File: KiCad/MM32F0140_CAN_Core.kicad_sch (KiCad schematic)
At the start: 1 part, among them U1 PIC32MX110F016D-IPT

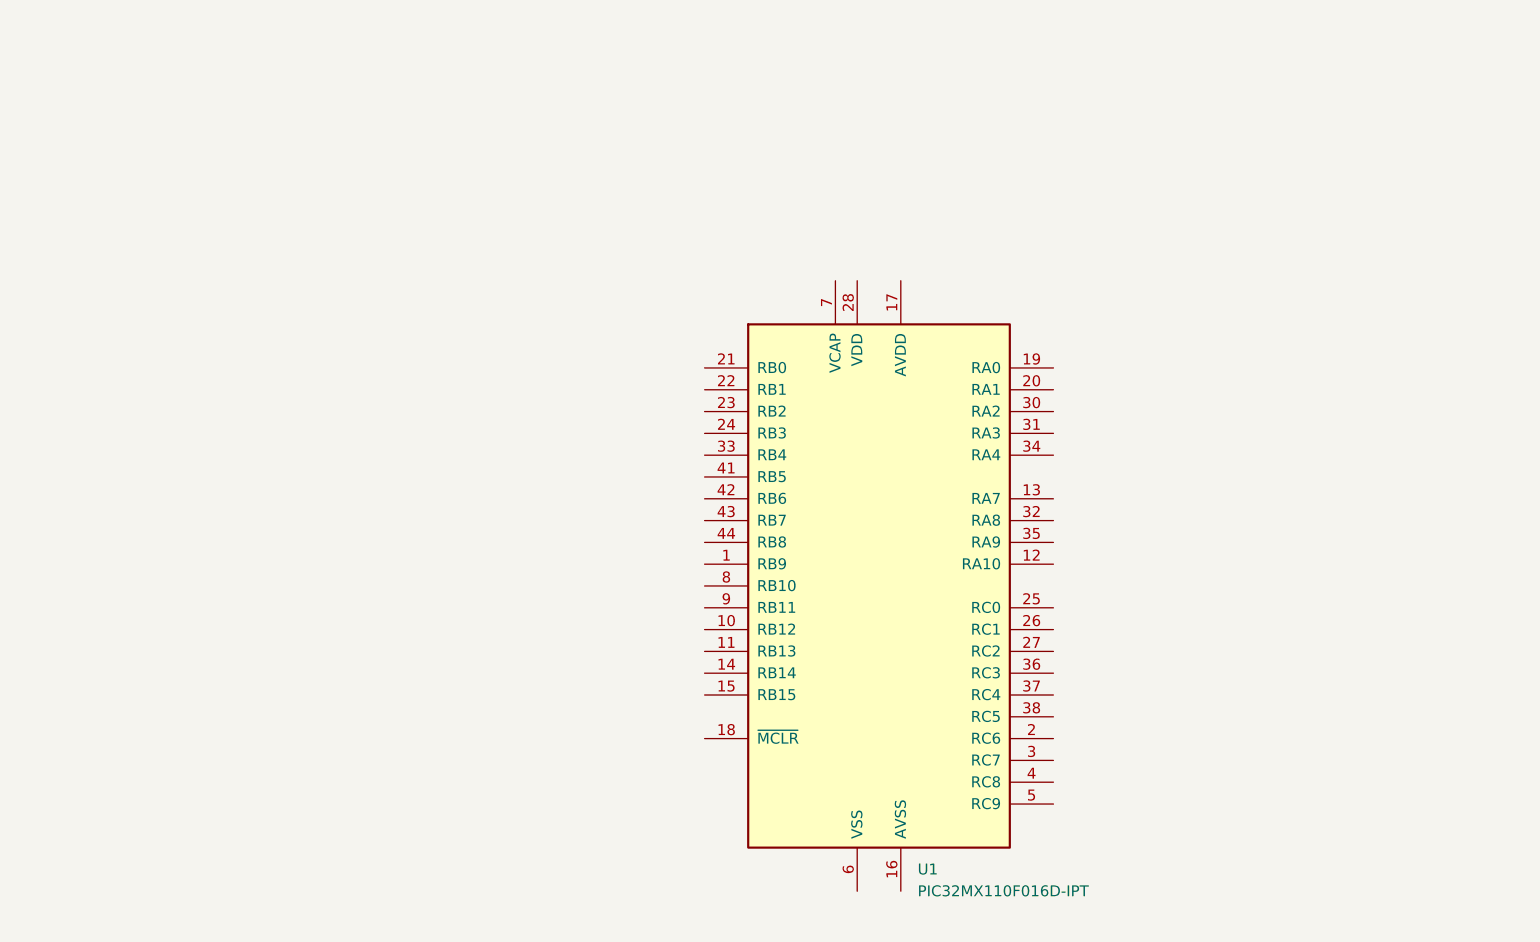
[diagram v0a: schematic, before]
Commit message: 更新原理图
23.4.7
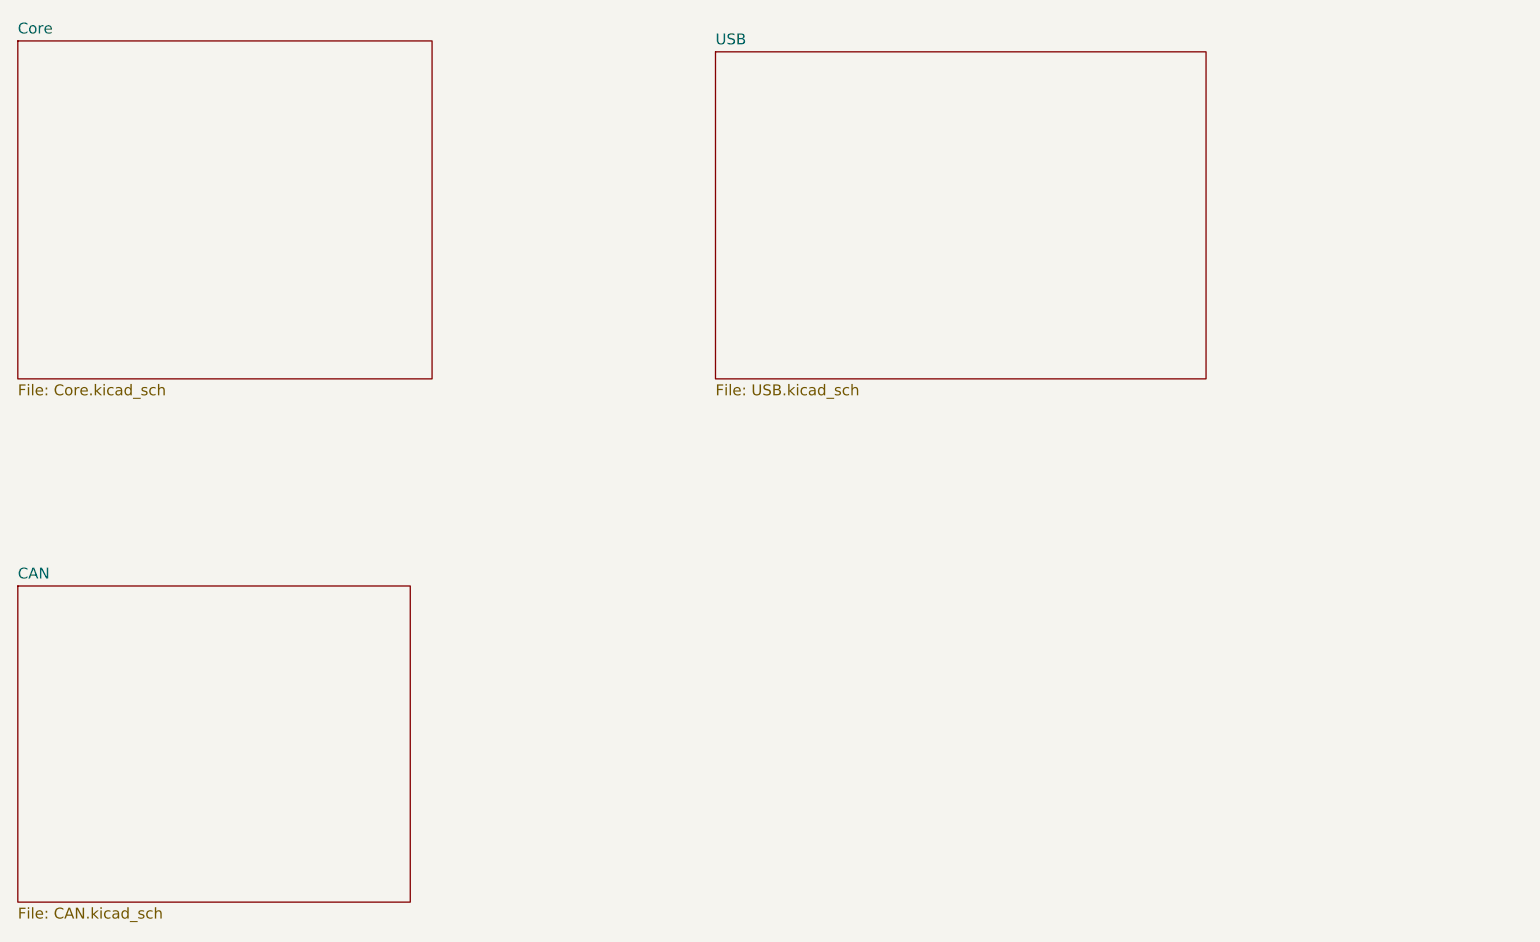
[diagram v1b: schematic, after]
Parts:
- removed U1: PIC32MX110F016D-IPT, Package_QFP:TQFP-44_10x10mm_P0.8mm, symbol MCU_Microchip_PIC32:PIC32MX110F016D-IPT
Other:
- added sheet CAN (CAN.kicad_sch)
- added sheet Core (Core.kicad_sch)
- added sheet USB (USB.kicad_sch)
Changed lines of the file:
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@@
 (kicad_sch (version 20230121) (generator eeschema)
   (paper "A4")
-  (symbol (lib_id "MCU_Microchip_PIC32:PIC32MX110F016D-IPT") (at 132.08 85.09 0) (unit 1)
-    (in_bom yes) (on_board yes) (dnp no) (fields_autoplaced)
-    (property "Reference" "U1" (at 136.5759 118.11 0)
-      (effects (font (size 1.27 1.27)) (justify left))
+  (sheet (at 31.75 85.09) (size 45.72 36.83) (fields_autoplaced)
+    (stroke (width 0.1524) (type solid))
+    (fill (color 0 0 0 0.0000))
+    (property "Sheetname" "CAN" (at 31.75 84.3784 0)
+      (effects (font (size 1.27 1.27)) (justify left bottom))
     )
-    (property "Value" "PIC32MX110F016D-IPT" (at 136.5759 120.65 0)
-      (effects (font (size 1.27 1.27)) (justify left))
+    (property "Sheetfile" "CAN.kicad_sch" (at 31.75 122.5046 0)
+      (effects (font (size 1.27 1.27)) (justify left top))
     )
-    (property "Footprint" "Package_QFP:TQFP-44_10x10mm_P0.8mm" (at 135.89 48.26 0)
-      (effects (font (size 1.27 1.27)) (justify left) hide)
-    )
-    (property "Datasheet" "http://ww1.microchip.com/downloads/en/DeviceDoc/60001168F.pdf" (at 132.08 90.17 0)
-      (effects (font (size 1.27 1.27)) hide)
-    )
-    (pin "1")
-    (pin "10")
-    (pin "11")
-    (pin "12")
-    (pin "13")
-    (pin "14")
-    (pin "15")
-    (pin "16")
-    (pin "17")
-    (pin "18")
-    (pin "19")
-    (pin "2")
-    (pin "20")
-    (pin "21")
-    (pin "22")
-    (pin "23")
-    (pin "24")
-    (pin "25")
-    (pin "26")
-    (pin "27")
-    (pin "28")
-    (pin "29")
-    (pin "3")
-    (pin "30")
-    (pin "31")
-    (pin "32")
-    (pin "33")
-    (pin "34")
-    (pin "35")
-    (pin "36")
-    (pin "37")
-    (pin "38")
-    (pin "39")
-    (pin "4")
-    (pin "40")
-    (pin "41")
-    (pin "42")
-    (pin "43")
-    (pin "44")
-    (pin "5")
-    (pin "6")
-    (pin "7")
-    (pin "8")
-    (pin "9")
     (instances
       (project "MM32F0140_CAN_Core"
-        (path "/325db86e-5883-4f53-9728-9eee822c47e5"
-          (reference "U1") (unit 1)
-        )
+        (path "/325db86e-5883-4f53-9728-9eee822c47e5" (page "4"))
       )
     )
+  )
+  (sheet (at 113.03 22.86) (size 57.15 38.1) (fields_autoplaced)
+    (stroke (width 0.1524) (type solid))
+    (fill (color 0 0 0 0.0000))
+    (property "Sheetname" "USB" (at 113.03 22.1484 0)
+      (effects (font (size 1.27 1.27)) (justify left bottom))
+    )
+    (property "Sheetfile" "USB.kicad_sch" (at 113.03 61.5446 0)
+      (effects (font (size 1.27 1.27)) (justify left top))
+    )
+    (instances
+      (project "MM32F0140_CAN_Core"
+        (path "/325db86e-5883-4f53-9728-9eee822c47e5" (page "3"))
+      )
+    )
+  )
+  (sheet (at 31.75 21.59) (size 48.26 39.37) (fields_autoplaced)
+    (stroke (width 0.1524) (type solid))
+    (fill (color 0 0 0 0.0000))
+    (property "Sheetname" "Core" (at 31.75 20.8784 0)
+      (effects (font (size 1.27 1.27)) (justify left bottom))
+    )
+    (property "Sheetfile" "Core.kicad_sch" (at 31.75 61.5446 0)
+      (effects (font (size 1.27 1.27)) (justify left top))
+    )
+    (instances
+      (project "MM32F0140_CAN_Core"
+        (path "/325db86e-5883-4f53-9728-9eee822c47e5" (page "2"))
+      )
+    )

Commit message: 更新原理图
2023.4.7 23:34
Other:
- sheet Core ports: added UART3_RX, UART3_TX; removed none
- sheet USB ports: added UART3_RX, UART3_TX; removed none
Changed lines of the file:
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@@
 (kicad_sch (version 20230121) (generator eeschema)
   (paper "A4")
+  (wire (pts (xy 80.01 34.29) (xy 113.03 34.29))
+    (stroke (width 0) (type default))
+  )
+  (wire (pts (xy 80.01 31.75) (xy 113.03 31.75))
+    (stroke (width 0) (type default))
+  )
   (sheet (at 31.75 85.09) (size 45.72 36.83) (fields_autoplaced)
     (stroke (width 0.1524) (type solid))
@@
       (effects (font (size 1.27 1.27)) (justify left top))
     )
+    (pin "UART3_RX" output (at 113.03 34.29 180)
+      (effects (font (size 1.27 1.27)) (justify left))
+    )
+    (pin "UART3_TX" input (at 113.03 31.75 180)
+      (effects (font (size 1.27 1.27)) (justify left))
+    )
     (instances
       (project "MM32F0140_CAN_Core"
@@
       (effects (font (size 1.27 1.27)) (justify left top))
     )
+    (pin "UART3_RX" input (at 80.01 34.29 0)
+      (effects (font (size 1.27 1.27)) (justify right))
+    )
+    (pin "UART3_TX" output (at 80.01 31.75 0)
+      (effects (font (size 1.27 1.27)) (justify right))
+    )
     (instances

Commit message: 原理图完成
2023.4.8:8:30
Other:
- sheet CAN ports: added CAN_RX, CAN_TX; removed none
- sheet Core ports: added CAN_RX, CAN_TX; removed none
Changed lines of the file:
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@@
 (kicad_sch (version 20230121) (generator eeschema)
   (paper "A4")
-  (wire (pts (xy 80.01 34.29) (xy 113.03 34.29))
+  (wire (pts (xy 116.84 104.14) (xy 149.86 104.14))
     (stroke (width 0) (type default))
   )
-  (wire (pts (xy 80.01 31.75) (xy 113.03 31.75))
+  (wire (pts (xy 116.84 77.47) (xy 149.86 77.47))
     (stroke (width 0) (type default))
   )
-  (sheet (at 31.75 85.09) (size 45.72 36.83) (fields_autoplaced)
+  (wire (pts (xy 116.84 74.93) (xy 149.86 74.93))
+    (stroke (width 0) (type default))
+  )
+  (wire (pts (xy 116.84 106.68) (xy 149.86 106.68))
+    (stroke (width 0) (type default))
+  )
+  (sheet (at 149.86 96.52) (size 57.15 22.86) (fields_autoplaced)
     (stroke (width 0.1524) (type solid))
     (fill (color 0 0 0 0.0000))
-    (property "Sheetname" "CAN" (at 31.75 84.3784 0)
+    (property "Sheetname" "CAN" (at 149.86 95.8084 0)
       (effects (font (size 1.27 1.27)) (justify left bottom))
     )
-    (property "Sheetfile" "CAN.kicad_sch" (at 31.75 122.5046 0)
+    (property "Sheetfile" "CAN.kicad_sch" (at 149.86 119.9646 0)
       (effects (font (size 1.27 1.27)) (justify left top))
+    )
+    (pin "CAN_TX" input (at 149.86 104.14 180)
+      (effects (font (size 1.27 1.27)) (justify left))
+    )
+    (pin "CAN_RX" output (at 149.86 106.68 180)
+      (effects (font (size 1.27 1.27)) (justify left))
     )
     (instances
@@
     )
   )
-  (sheet (at 113.03 22.86) (size 57.15 38.1) (fields_autoplaced)
+  (sheet (at 149.86 66.04) (size 57.15 22.86) (fields_autoplaced)
     (stroke (width 0.1524) (type solid))
     (fill (color 0 0 0 0.0000))
-    (property "Sheetname" "USB" (at 113.03 22.1484 0)
+    (property "Sheetname" "USB" (at 149.86 65.3284 0)
       (effects (font (size 1.27 1.27)) (justify left bottom))
     )
-    (property "Sheetfile" "USB.kicad_sch" (at 113.03 61.5446 0)
+    (property "Sheetfile" "USB.kicad_sch" (at 149.86 89.4846 0)
       (effects (font (size 1.27 1.27)) (justify left top))
     )
-    (pin "UART3_RX" output (at 113.03 34.29 180)
+    (pin "UART3_RX" output (at 149.86 77.47 180)
       (effects (font (size 1.27 1.27)) (justify left))
     )
-    (pin "UART3_TX" input (at 113.03 31.75 180)
+    (pin "UART3_TX" input (at 149.86 74.93 180)
       (effects (font (size 1.27 1.27)) (justify left))
     )
@@
     )
   )
-  (sheet (at 31.75 21.59) (size 48.26 39.37) (fields_autoplaced)
+  (sheet (at 68.58 64.77) (size 48.26 55.88) (fields_autoplaced)
     (stroke (width 0.1524) (type solid))
     (fill (color 0 0 0 0.0000))
-    (property "Sheetname" "Core" (at 31.75 20.8784 0)
+    (property "Sheetname" "Core" (at 68.58 64.0584 0)
       (effects (font (size 1.27 1.27)) (justify left bottom))
     )
-    (property "Sheetfile" "Core.kicad_sch" (at 31.75 61.5446 0)
+    (property "Sheetfile" "Core.kicad_sch" (at 68.58 121.2346 0)
       (effects (font (size 1.27 1.27)) (justify left top))
     )
-    (pin "UART3_RX" input (at 80.01 34.29 0)
+    (pin "UART3_RX" input (at 116.84 77.47 0)
       (effects (font (size 1.27 1.27)) (justify right))
     )
-    (pin "UART3_TX" output (at 80.01 31.75 0)
+    (pin "UART3_TX" output (at 116.84 74.93 0)
       (effects (font (size 1.27 1.27)) (justify right))
     )
+    (pin "CAN_TX" output (at 116.84 104.14 0)
+      (effects (font (size 1.27 1.27)) (justify right))
+    )
+    (pin "CAN_RX" input (at 116.84 106.68 0)
+      (effects (font (size 1.27 1.27)) (justify right))
+    )
